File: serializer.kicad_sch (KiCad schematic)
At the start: 29 parts

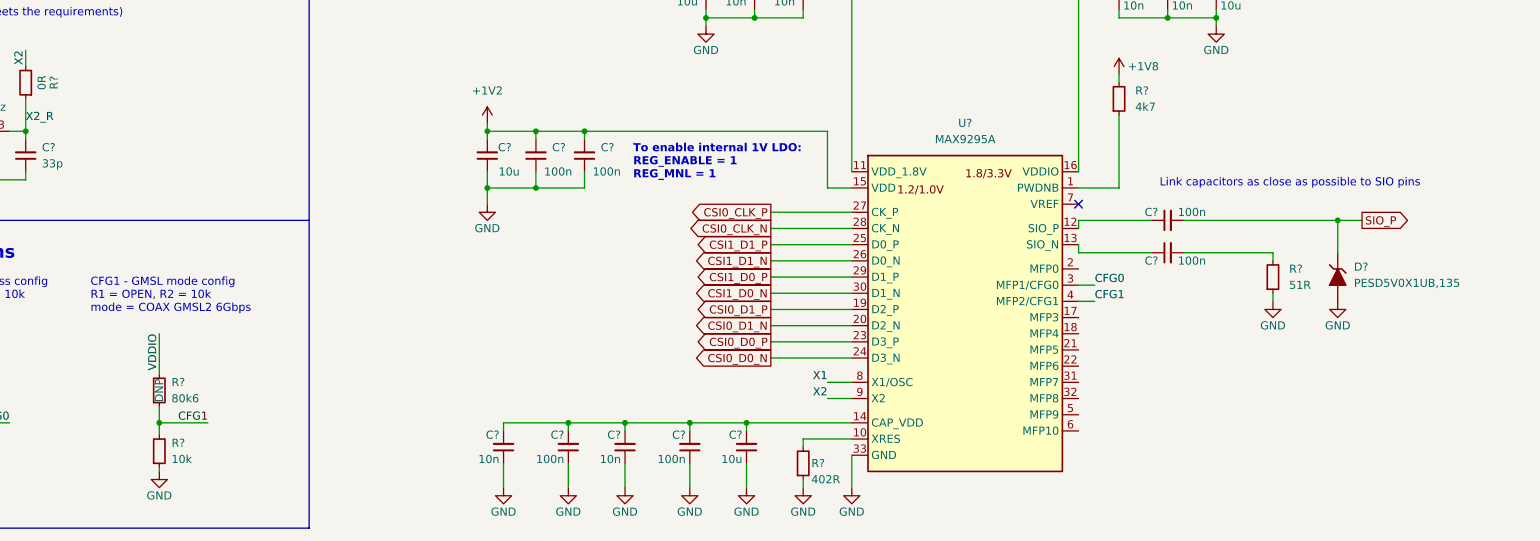
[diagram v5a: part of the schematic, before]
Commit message: Add i2c and gpio triggers
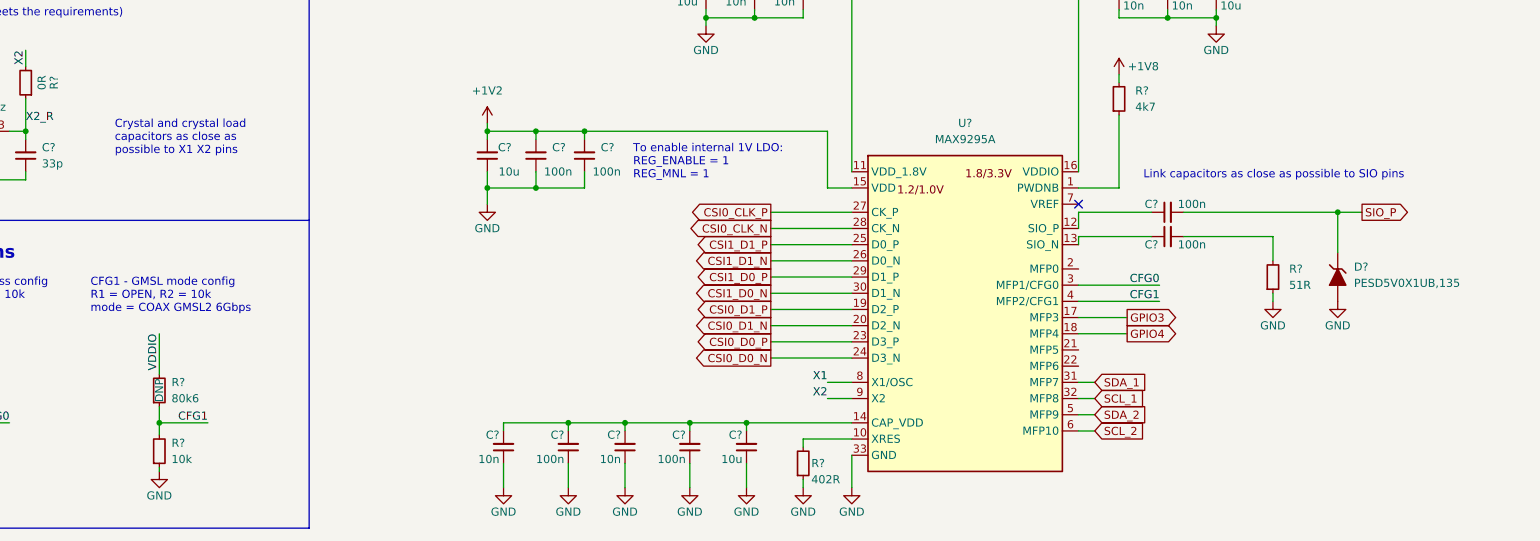
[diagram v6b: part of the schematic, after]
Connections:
- net GPIO3: now reaches U?.17 (MFP3)
- net GPIO4: now reaches U?.18 (MFP4)
- net SDA_1: now reaches U?.31 (MFP7)
- net SCL_1: now reaches U?.32 (MFP8)
- net SDA_2: now reaches U?.5 (MFP9)
- net SCL_2: now reaches U?.6 (MFP10)
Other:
- note added: "Crystal and crystal load capacitors as close as possible to X1 X2 pins"
- moved on the sheet: C?

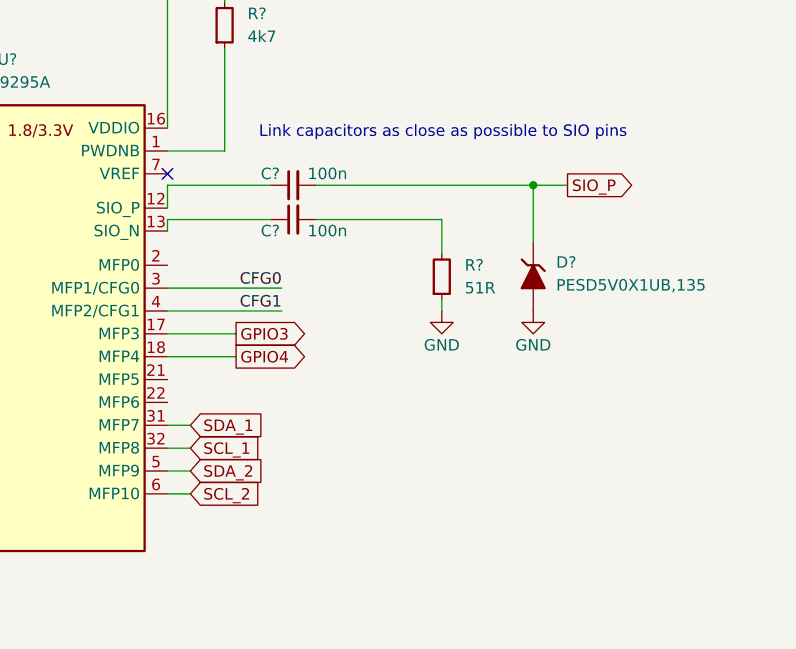
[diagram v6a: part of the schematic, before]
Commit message: Add resistor selectable i2c
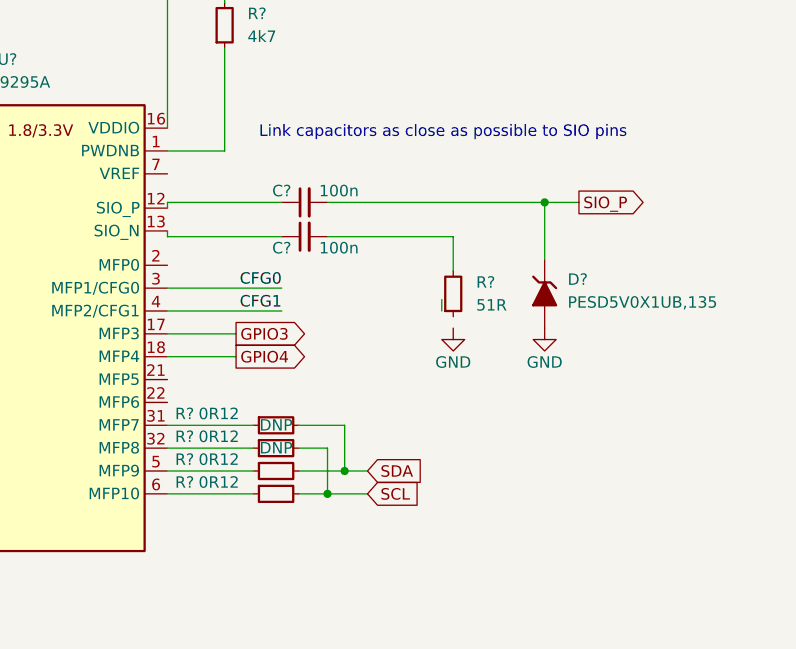
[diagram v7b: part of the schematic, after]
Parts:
- added R? (x4): R_0R12_0402, antmicro-footprints:R_0402_1005Metric, symbol antmicroResistors0402:R_0R12_0402
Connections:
- net GND: no longer R?.1
- net SCL_1: no longer names the net of U?.32 (MFP8)
- net SCL_1: now also R?.1
- net SCL_2: no longer names the net of U?.6 (MFP10)
- net SCL_2: now also R?.1
- net SDA_1: no longer names the net of U?.31 (MFP7)
- net SDA_1: now also R?.1
- net SDA_2: no longer names the net of U?.5 (MFP9)
- net SDA_2: now also R?.1
- new net SCL: R?.2, R?.2
- new net SDA: R?.2, R?.2
- no-connect marks 1 -> 0
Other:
- moved on the sheet: C?, D?, R?

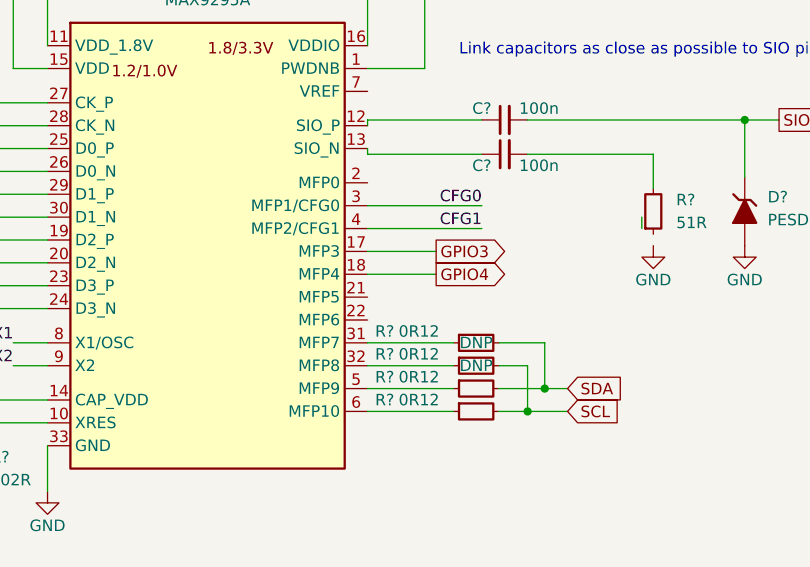
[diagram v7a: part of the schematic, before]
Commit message: Add testpoints to unused MF pins
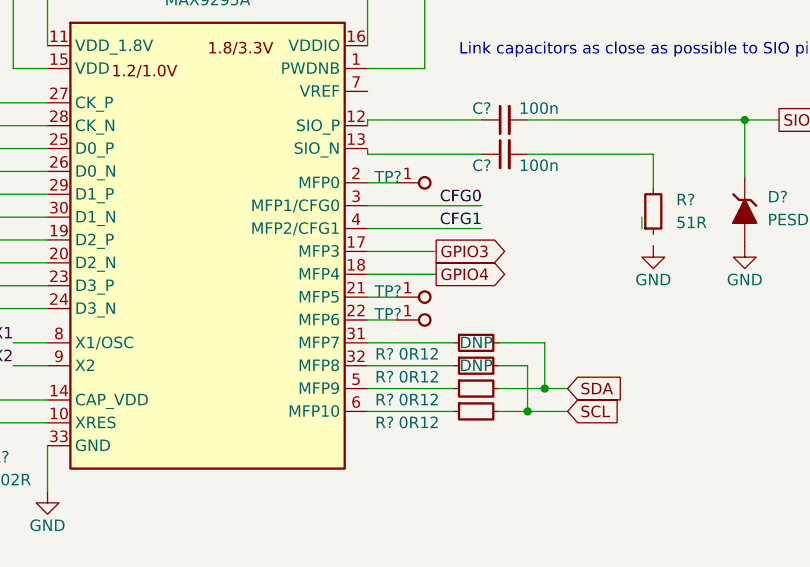
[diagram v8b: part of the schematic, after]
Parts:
- added TP? (x3): TP_1.5mm_SMD, antmicro-footprints:TP_SMD_1.5mm, symbol antmicroTestPoints:TP_1.5mm_SMD
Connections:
- net at U?.2 (MFP0): now also TP?.1
- net at U?.21 (MFP5): now also TP?.1
- net at U?.22 (MFP6): now also TP?.1
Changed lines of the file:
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@@
     (stroke (width 0) (type default) (color 0 0 0 0))
   )
+  (wire (pts (xy 198.12 97.79) (xy 201.295 97.79))
+    (stroke (width 0) (type default) (color 0 0 0 0))
+  )
   (wire (pts (xy 212.725 105.41) (xy 215.9 105.41))
     (stroke (width 0) (type default) (color 0 0 0 0))
   )
+  (wire (pts (xy 198.12 85.09) (xy 201.295 85.09))
+    (stroke (width 0) (type default) (color 0 0 0 0))
+  )
   (wire (pts (xy 105.41 63.5) (xy 113.03 63.5))
     (stroke (width 0) (type default) (color 0 0 0 0))
@@
     (stroke (width 0) (type default) (color 0 0 0 0))
   )
+  (wire (pts (xy 198.12 100.33) (xy 201.295 100.33))
+    (stroke (width 0) (type default) (color 0 0 0 0))
+  )
   (wire (pts (xy 204.47 54.61) (xy 204.47 55.88))
     (stroke (width 0) (type default) (color 0 0 0 0))
@@
   (symbol (lib_id "antmicroResistors0402:R_0R12_0402") (at 207.645 110.49 0) (unit 1)
     (in_bom yes) (on_board yes)
-    (property "Reference" "R?" (id 0) (at 200.025 109.22 0)
+    (property "Reference" "R?" (id 0) (at 200.025 111.76 0)
       (effects (font (size 1.27 1.27) (thickness 0.15)))
     )
@@
       (effects (font (size 1.27 1.27) (thickness 0.15)) (justify left bottom) hide)
     )
-    (property "Val" "0R12" (id 8) (at 203.835 109.22 0)
+    (property "Val" "0R12" (id 8) (at 203.835 111.76 0)
       (effects (font (size 1.27 1.27) (thickness 0.15)))
     )
@@
     (pin "2")
   )
+  (symbol (lib_id "antmicroTestPoints:TP_1.5mm_SMD") (at 201.295 97.79 0) (unit 1)
+    (in_bom yes) (on_board yes)
+    (property "Reference" "TP?" (id 0) (at 201.93 97.155 0)
+      (effects (font (size 1.27 1.27) (thickness 0.15)) (justify right))
+    )
+    (property "Value" "TP_1.5mm_SMD" (id 1) (at 216.535 105.41 0)
+      (effects (font (size 1.27 1.27) (thickness 0.15)) (justify left bottom) hide)
+    )
+    (property "Footprint" "antmicro-footprints:TP_SMD_1.5mm" (id 2) (at 216.535 107.95 0)
+      (effects (font (size 1.27 1.27) (thickness 0.15)) (justify left bottom) hide)
+    )
+    (property "Datasheet" "" (id 3) (at 219.075 110.49 0)
+      (effects (font (size 1.27 1.27) (thickness 0.15)) (justify left bottom) hide)
+    )
+    (property "MPN" "" (id 4) (at 201.295 97.79 0)
+      (effects (font (size 1.27 1.27)) hide)
+    )
+    (property "Manufacturer" "" (id 5) (at 201.295 97.79 0)
+      (effects (font (size 1.27 1.27)) hide)
+    )
+    (property "Author" "Antmicro" (id 6) (at 216.535 113.03 0)
+      (effects (font (size 1.27 1.27) (thickness 0.15)) (justify left bottom) hide)
+    )
+    (property "License" "Apache-2.0" (id 7) (at 216.535 115.57 0)
+      (effects (font (size 1.27 1.27) (thickness 0.15)) (justify left bottom) hide)
+    )
+    (pin "1")
+  )
+  (symbol (lib_id "antmicroTestPoints:TP_1.5mm_SMD") (at 201.295 100.33 0) (unit 1)
+    (in_bom yes) (on_board yes)
+    (property "Reference" "TP?" (id 0) (at 201.93 99.695 0)
+      (effects (font (size 1.27 1.27) (thickness 0.15)) (justify right))
+    )
+    (property "Value" "TP_1.5mm_SMD" (id 1) (at 216.535 107.95 0)
+      (effects (font (size 1.27 1.27) (thickness 0.15)) (justify left bottom) hide)
+    )
+    (property "Footprint" "antmicro-footprints:TP_SMD_1.5mm" (id 2) (at 216.535 110.49 0)
+      (effects (font (size 1.27 1.27) (thickness 0.15)) (justify left bottom) hide)
+    )
+    (property "Datasheet" "" (id 3) (at 219.075 113.03 0)
+      (effects (font (size 1.27 1.27) (thickness 0.15)) (justify left bottom) hide)
+    )
+    (property "MPN" "" (id 4) (at 201.295 100.33 0)
+      (effects (font (size 1.27 1.27)) hide)
+    )
+    (property "Manufacturer" "" (id 5) (at 201.295 100.33 0)
+      (effects (font (size 1.27 1.27)) hide)
+    )
+    (property "Author" "Antmicro" (id 6) (at 216.535 115.57 0)
+      (effects (font (size 1.27 1.27) (thickness 0.15)) (justify left bottom) hide)
+    )
+    (property "License" "Apache-2.0" (id 7) (at 216.535 118.11 0)
+      (effects (font (size 1.27 1.27) (thickness 0.15)) (justify left bottom) hide)
+    )
+    (pin "1")
+  )
   (symbol (lib_id "antmicroCapacitors0402:C_100n_0402") (at 118.11 115.57 270) (mirror x) (unit 1)
     (in_bom yes) (on_board yes)
@@
   (symbol (lib_id "antmicroResistors0402:R_0R12_0402") (at 207.645 107.95 0) (unit 1)
     (in_bom yes) (on_board yes)
-    (property "Reference" "R?" (id 0) (at 200.025 106.68 0)
+    (property "Reference" "R?" (id 0) (at 200.025 109.22 0)
       (effects (font (size 1.27 1.27) (thickness 0.15)))
     )
@@
       (effects (font (size 1.27 1.27) (thickness 0.15)) (justify left bottom) hide)
     )
-    (property "Val" "0R12" (id 8) (at 203.835 106.68 0)
+    (property "Val" "0R12" (id 8) (at 203.835 109.22 0)
       (effects (font (size 1.27 1.27) (thickness 0.15)))
     )
@@
     (pin "1")
   )
+  (symbol (lib_id "antmicroTestPoints:TP_1.5mm_SMD") (at 201.295 85.09 0) (unit 1)
+    (in_bom yes) (on_board yes)
+    (property "Reference" "TP?" (id 0) (at 201.93 84.455 0)
+      (effects (font (size 1.27 1.27) (thickness 0.15)) (justify right))
+    )
+    (property "Value" "TP_1.5mm_SMD" (id 1) (at 216.535 92.71 0)
+      (effects (font (size 1.27 1.27) (thickness 0.15)) (justify left bottom) hide)
+    )
+    (property "Footprint" "antmicro-footprints:TP_SMD_1.5mm" (id 2) (at 216.535 95.25 0)
+      (effects (font (size 1.27 1.27) (thickness 0.15)) (justify left bottom) hide)
+    )
+    (property "Datasheet" "" (id 3) (at 219.075 97.79 0)
+      (effects (font (size 1.27 1.27) (thickness 0.15)) (justify left bottom) hide)
+    )
+    (property "MPN" "" (id 4) (at 201.295 85.09 0)
+      (effects (font (size 1.27 1.27)) hide)
+    )
+    (property "Manufacturer" "" (id 5) (at 201.295 85.09 0)
+      (effects (font (size 1.27 1.27)) hide)
+    )
+    (property "Author" "Antmicro" (id 6) (at 216.535 100.33 0)
+      (effects (font (size 1.27 1.27) (thickness 0.15)) (justify left bottom) hide)
+    )
+    (property "License" "Apache-2.0" (id 7) (at 216.535 102.87 0)
+      (effects (font (size 1.27 1.27) (thickness 0.15)) (justify left bottom) hide)
+    )
+    (pin "1")
+  )
   (symbol (lib_id "antmicroTVSDiodes:PESD5V0X1UB") (at 240.03 92.075 90) (unit 1)
     (in_bom yes) (on_board yes) (fields_autoplaced)
@@
   (symbol (lib_id "antmicroResistors0402:R_0R12_0402") (at 207.645 102.87 0) (unit 1)
     (in_bom yes) (on_board yes)
-    (property "Reference" "R?" (id 0) (at 200.025 101.6 0)
+    (property "Reference" "R?" (id 0) (at 200.025 104.14 0)
       (effects (font (size 1.27 1.27) (thickness 0.15)))
     )
@@
       (effects (font (size 1.27 1.27) (thickness 0.15)) (justify left bottom) hide)
     )
-    (property "Val" "0R12" (id 8) (at 203.835 101.6 0)
+    (property "Val" "0R12" (id 8) (at 203.835 104.14 0)
       (effects (font (size 1.27 1.27) (thickness 0.15)))
     )
@@
   (symbol (lib_id "antmicroResistors0402:R_0R12_0402") (at 207.645 105.41 0) (unit 1)
     (in_bom yes) (on_board yes)
-    (property "Reference" "R?" (id 0) (at 200.025 104.14 0)
+    (property "Reference" "R?" (id 0) (at 200.025 106.68 0)
       (effects (font (size 1.27 1.27) (thickness 0.15)))
     )
@@
       (effects (font (size 1.27 1.27) (thickness 0.15)) (justify left bottom) hide)
     )
-    (property "Val" "0R12" (id 8) (at 203.835 104.14 0)
+    (property "Val" "0R12" (id 8) (at 203.835 106.68 0)
       (effects (font (size 1.27 1.27) (thickness 0.15)))
     )
